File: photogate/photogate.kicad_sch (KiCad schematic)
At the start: 13 parts, among them P2_Jack_F(Leds)1 SJ1-3525N

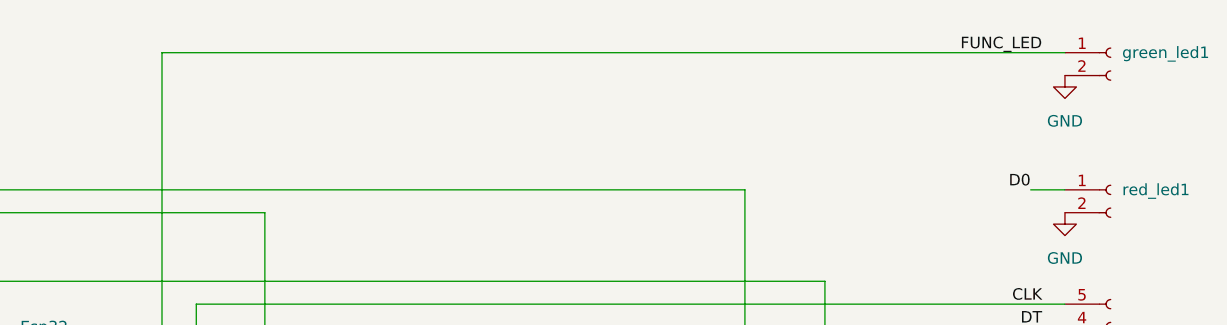
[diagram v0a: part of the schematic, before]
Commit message: Add resitor green led
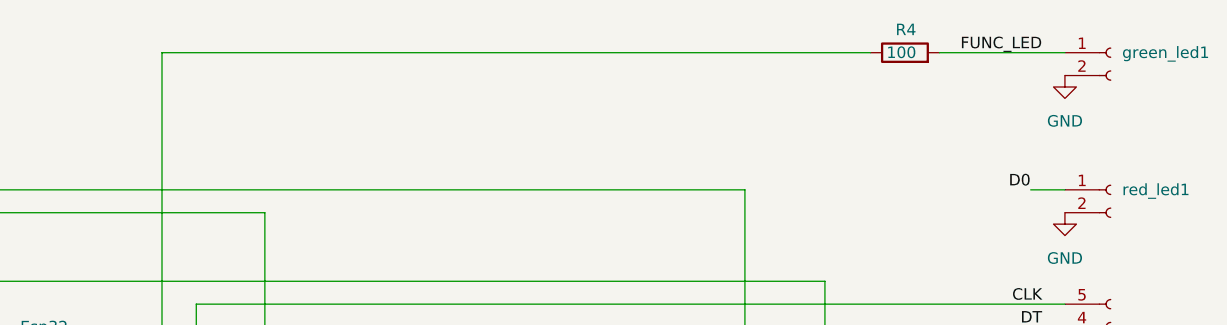
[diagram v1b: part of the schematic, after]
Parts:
- added R4: 100, Resistor_THT:R_Axial_DIN0204_L3.6mm_D1.6mm_P5.08mm_Horizontal, symbol Device:R
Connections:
- net FUNC_LED: now also R4.2; no longer Esp32.6 (IO32)
- new net: Esp32.6 (IO32), R4.1
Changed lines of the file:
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@@
     (stroke (width 0) (type default) (color 0 0 0 0))
   )
-  (wire (pts (xy 97.79 43.18) (xy 198.12 43.18))
+  (wire (pts (xy 97.79 43.18) (xy 176.53 43.18))
     (stroke (width 0) (type default) (color 0 0 0 0))
   )
   (wire (pts (xy 105.41 73.66) (xy 198.12 73.66))
+    (stroke (width 0) (type default) (color 0 0 0 0))
+  )
+  (wire (pts (xy 184.15 43.18) (xy 198.12 43.18))
     (stroke (width 0) (type default) (color 0 0 0 0))
   )
@@
     (pin "4")
   )
+  (symbol (lib_id "Device:R") (at 180.34 43.18 90) (unit 1)
+    (in_bom yes) (on_board yes)
+    (property "Reference" "R4" (id 0) (at 181.61 40.64 90)
+      (effects (font (size 1.27 1.27)) (justify left))
+    )
+    (property "Value" "100" (id 1) (at 181.61 43.18 90)
+      (effects (font (size 1.27 1.27)) (justify left))
+    )
+    (property "Footprint" "Resistor_THT:R_Axial_DIN0204_L3.6mm_D1.6mm_P5.08mm_Horizontal" (id 2) (at 180.34 44.958 90)
+      (effects (font (size 1.27 1.27)) hide)
+    )
+    (property "Datasheet" "~" (id 3) (at 180.34 43.18 0)
+      (effects (font (size 1.27 1.27)) hide)
+    )
+    (pin "1")
+    (pin "2")
+  )
   (symbol (lib_id "Connector:Conn_01x02_Female") (at 203.2 58.42 0) (unit 1)
     (in_bom yes) (on_board yes) (fields_autoplaced)
@@
       (reference "R3") (unit 1) (value "100") (footprint "Resistor_THT:R_Axial_DIN0204_L3.6mm_D1.6mm_P5.08mm_Horizontal")
     )
+    (path "/548078db-cb79-4624-8d94-1114d4729585"
+      (reference "R4") (unit 1) (value "100") (footprint "Resistor_THT:R_Axial_DIN0204_L3.6mm_D1.6mm_P5.08mm_Horizontal")
+    )
     (path "/63f1f18f-ec45-4294-bfb1-f0f704a6258f"

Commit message: Melhoras na placa
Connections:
- net D0: now also red_led1.2 (Pin_2); no longer red_led1.1 (Pin_1)
- net FUNC_LED: now also green_led1.2 (Pin_2); no longer green_led1.1 (Pin_1)
- net GND: now also green_led1.1 (Pin_1), red_led1.1 (Pin_1); no longer Esp32.17 (GND), green_led1.2 (Pin_2), red_led1.2 (Pin_2)
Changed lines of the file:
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@@
   (junction (at 198.12 110.49) (diameter 0) (color 0 0 0 0)
   )
-  (junction (at 80.01 147.32) (diameter 0) (color 0 0 0 0)
-  )
   (junction (at 171.45 124.46) (diameter 0) (color 0 0 0 0)
   )
@@
     (stroke (width 0) (type default) (color 0 0 0 0))
   )
+  (wire (pts (xy 194.31 58.42) (xy 198.12 58.42))
+    (stroke (width 0) (type default) (color 0 0 0 0))
+  )
   (wire (pts (xy 149.86 124.46) (xy 171.45 124.46))
     (stroke (width 0) (type default) (color 0 0 0 0))
   )
+  (wire (pts (xy 184.15 43.18) (xy 198.12 43.18))
+    (stroke (width 0) (type default) (color 0 0 0 0))
+  )
   (wire (pts (xy 198.12 110.49) (xy 198.12 113.03))
     (stroke (width 0) (type default) (color 0 0 0 0))
@@
     (stroke (width 0) (type default) (color 0 0 0 0))
   )
-  (wire (pts (xy 77.47 147.32) (xy 80.01 147.32))
+  (wire (pts (xy 77.47 147.32) (xy 139.7 147.32))
     (stroke (width 0) (type default) (color 0 0 0 0))
   )
@@
     (stroke (width 0) (type default) (color 0 0 0 0))
   )
-  (wire (pts (xy 184.15 43.18) (xy 198.12 43.18))
-    (stroke (width 0) (type default) (color 0 0 0 0))
-  )
   (wire (pts (xy 198.12 127) (xy 198.12 129.54))
     (stroke (width 0) (type default) (color 0 0 0 0))
@@
     (stroke (width 0) (type default) (color 0 0 0 0))
   )
-  (wire (pts (xy 194.31 58.42) (xy 198.12 58.42))
-    (stroke (width 0) (type default) (color 0 0 0 0))
-  )
   (wire (pts (xy 139.7 124.46) (xy 139.7 127))
     (stroke (width 0) (type default) (color 0 0 0 0))
   )
   (wire (pts (xy 95.25 137.16) (xy 105.41 137.16))
-    (stroke (width 0) (type default) (color 0 0 0 0))
-  )
-  (wire (pts (xy 80.01 147.32) (xy 139.7 147.32))
     (stroke (width 0) (type default) (color 0 0 0 0))
   )
@@
     (pin "2")
   )
-  (symbol (lib_id "Connector:Conn_01x02_Female") (at 203.2 58.42 0) (unit 1)
-    (in_bom yes) (on_board yes) (fields_autoplaced)
-    (property "Reference" "red_led1" (id 0) (at 204.47 58.4199 0)
-      (effects (font (size 1.27 1.27)) (justify left))
-    )
-    (property "Value" "Conn_01x02_Female" (id 1) (at 204.47 60.9599 0)
+  (symbol (lib_id "Connector:Conn_01x02_Female") (at 203.2 60.96 0) (mirror x) (unit 1)
+    (in_bom yes) (on_board yes) (fields_autoplaced)
+    (property "Reference" "red_led1" (id 0) (at 202.565 55.88 0))
+    (property "Value" "Conn_01x02_Female" (id 1) (at 204.47 58.4201 0)
       (effects (font (size 1.27 1.27)) (justify left) hide)
     )
-    (property "Footprint" "Connector_JST:JST_EH_B2B-EH-A_1x02_P2.50mm_Vertical" (id 2) (at 203.2 58.42 0)
-      (effects (font (size 1.27 1.27)) hide)
-    )
-    (property "Datasheet" "~" (id 3) (at 203.2 58.42 0)
+    (property "Footprint" "Connector_JST:JST_EH_B2B-EH-A_1x02_P2.50mm_Vertical" (id 2) (at 203.2 60.96 0)
+      (effects (font (size 1.27 1.27)) hide)
+    )
+    (property "Datasheet" "~" (id 3) (at 203.2 60.96 0)
       (effects (font (size 1.27 1.27)) hide)
     )
@@
     (pin "1")
   )
-  (symbol (lib_id "Connector:Conn_01x02_Female") (at 203.2 43.18 0) (unit 1)
-    (in_bom yes) (on_board yes)
-    (property "Reference" "green_led1" (id 0) (at 204.47 43.18 0)
-      (effects (font (size 1.27 1.27)) (justify left))
-    )
-    (property "Value" "Conn_01x02_Female" (id 1) (at 204.47 45.7199 0)
+  (symbol (lib_id "Connector:Conn_01x02_Female") (at 203.2 45.72 0) (mirror x) (unit 1)
+    (in_bom yes) (on_board yes)
+    (property "Reference" "green_led1" (id 0) (at 209.55 45.72 0)
+      (effects (font (size 1.27 1.27)) (justify left))
+    )
+    (property "Value" "Conn_01x02_Female" (id 1) (at 204.47 43.1801 0)
       (effects (font (size 1.27 1.27)) (justify left) hide)
     )
-    (property "Footprint" "Connector_JST:JST_EH_B2B-EH-A_1x02_P2.50mm_Vertical" (id 2) (at 203.2 43.18 0)
-      (effects (font (size 1.27 1.27)) hide)
-    )
-    (property "Datasheet" "~" (id 3) (at 203.2 43.18 0)
-      (effects (font (size 1.27 1.27)) hide)
-    )
+    (property "Footprint" "Connector_JST:JST_EH_B2B-EH-A_1x02_P2.50mm_Vertical" (id 2) (at 203.2 45.72 0)
+      (effects (font (size 1.27 1.27)) hide)
+    )
+    (property "Datasheet" "~" (id 3) (at 203.2 45.72 0)
+      (effects (font (size 1.27 1.27)) hide)
+    )

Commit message: att designe PCB
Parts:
- removed P2_Jack_F(Leds)1: SJ1-3525N, MyFootprints:CUI_SJ1-3525N, symbol Jacks:SJ1-3525N
- added P2jack1: SJ1-3515N, MyFootprints:CUI_SJ1-3515N, symbol MySymbols:SJ1-3515N
- added R5: 470, Resistor_THT:R_Axial_DIN0204_L3.6mm_D1.6mm_P7.62mm_Horizontal, symbol Device:R
- C1: value 104 -> 104k; footprint Capacitor_THT:C_Disc_D5.1mm_W3.2mm_P5.00mm -> Capacitor_THT:C_Disc_D10.5mm_W5.0mm_P10.00mm
- LM393N_A1: value LM393N_A -> LM393N1
- R1: renamed from R4; footprint Resistor_THT:R_Axial_DIN0204_L3.6mm_D1.6mm_P5.08mm_Horizontal -> Resistor_THT:R_Axial_DIN0204_L3.6mm_D1.6mm_P7.62mm_Horizontal
- R2: renamed from R3; footprint Resistor_THT:R_Axial_DIN0204_L3.6mm_D1.6mm_P5.08mm_Horizontal -> Resistor_THT:R_Axial_DIN0204_L3.6mm_D1.6mm_P7.62mm_Horizontal
- R3: renamed from R1; footprint Resistor_THT:R_Axial_DIN0204_L3.6mm_D1.6mm_P5.08mm_Horizontal -> Resistor_THT:R_Axial_DIN0204_L3.6mm_D1.6mm_P7.62mm_Horizontal
- R4: renamed from R2; footprint Resistor_THT:R_Axial_DIN0204_L3.6mm_D1.6mm_P5.08mm_Horizontal -> Resistor_THT:R_Axial_DIN0204_L3.6mm_D1.6mm_P7.62mm_Horizontal
- renumbered VR10kteste1 to VR1
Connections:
- net D0: now also R5.1; no longer red_led1.2 (Pin_2)
- net GND: now also Esp32.17 (GND), P2jack1.2, P2jack1.4
- net PHOTODIODE: now also P2jack1.1
- net at Esp32.15 (VIN), Jack_5V1.4, R3.1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: no longer C1.1, LM393N_A1.8 (V+), R2.2, R4.1, VR1.1
- net at Esp32.16 (3V3): now also C1.1, LM393N_A1.8 (V+), R4.1, VR1.1, R5.2
- net at R3.2: now also P2jack1.3, P2jack1.5
- new net: R2.2, red_led1.2 (Pin_2)
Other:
- moved on the sheet: R2, R4, VR1

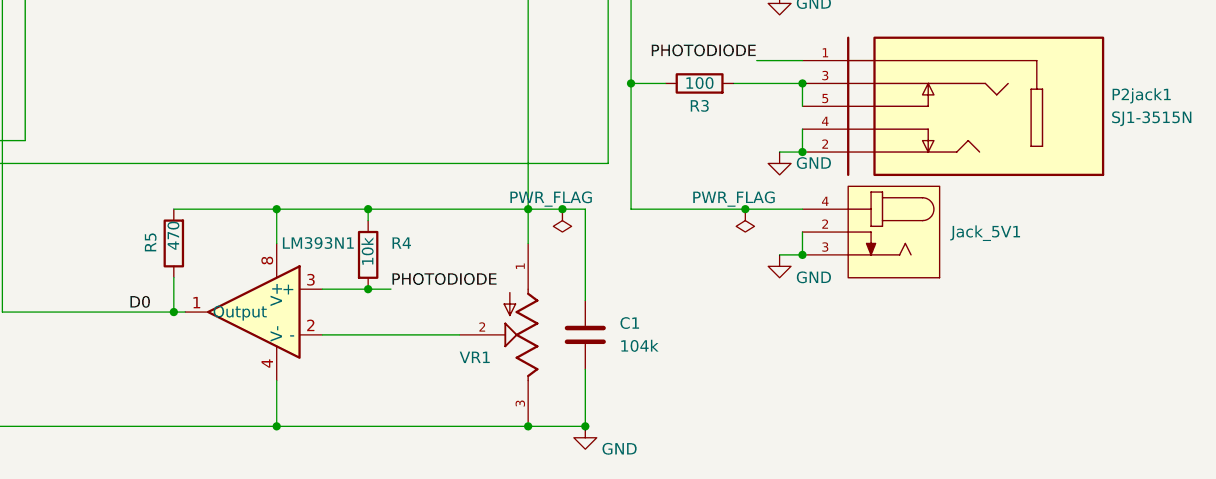
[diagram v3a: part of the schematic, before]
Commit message: Add connector para switch
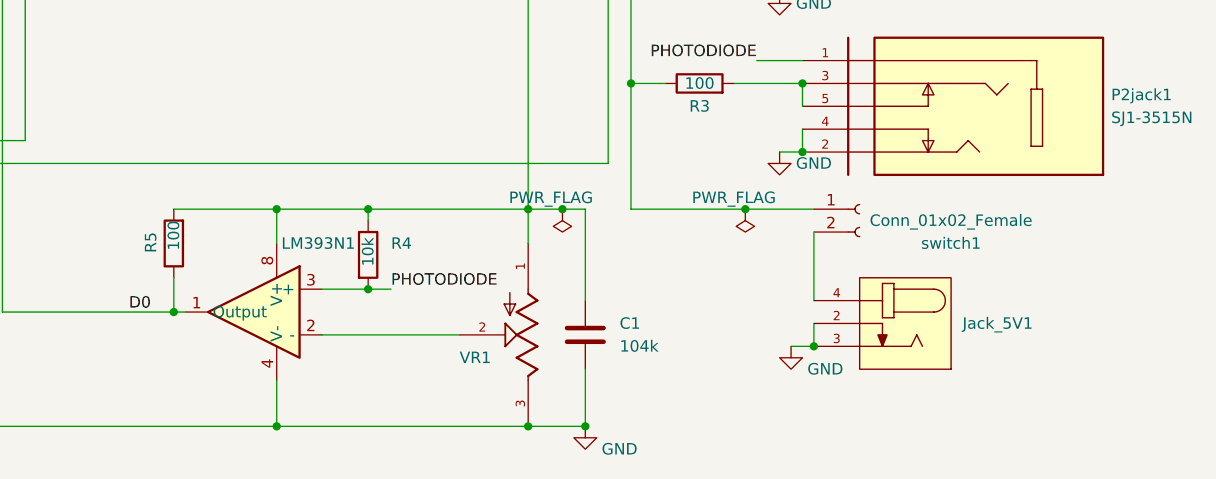
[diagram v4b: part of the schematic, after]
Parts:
- added switch1: Conn_01x02_Female, Connector_JST:JST_EH_B2B-EH-A_1x02_P2.50mm_Vertical, symbol Connector:Conn_01x02_Female
- R5: value 470 -> 100
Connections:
- net at Esp32.15 (VIN), R3.1, display1.2 (Pin_2)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: now also switch1.1 (Pin_1); no longer Jack_5V1.4
- new net: Jack_5V1.4, switch1.2 (Pin_2)
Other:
- moved on the sheet: Jack_5V1
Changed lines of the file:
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@@
   (junction (at 179.07 78.74) (diameter 0) (color 0 0 0 0)
   )
-  (junction (at 198.12 129.54) (diameter 0) (color 0 0 0 0)
+  (junction (at 199.39 139.7) (diameter 0) (color 0 0 0 0)
   )
   (junction (at 139.7 148.59) (diameter 0) (color 0 0 0 0)
@@
   (junction (at 167.64 148.59) (diameter 0) (color 0 0 0 0)
   )
+  (junction (at 198.12 118.11) (diameter 0) (color 0 0 0 0)
+  )
+  (junction (at 77.47 147.32) (diameter 0) (color 0 0 0 0)
+  )
+  (junction (at 173.99 148.59) (diameter 0) (color 0 0 0 0)
+  )
   (junction (at 191.77 124.46) (diameter 0) (color 0 0 0 0)
   )
-  (junction (at 198.12 118.11) (diameter 0) (color 0 0 0 0)
-  )
-  (junction (at 77.47 147.32) (diameter 0) (color 0 0 0 0)
-  )
-  (junction (at 173.99 148.59) (diameter 0) (color 0 0 0 0)
-  )
   (junction (at 167.64 124.46) (diameter 0) (color 0 0 0 0)
   )
@@
     (stroke (width 0) (type default) (color 0 0 0 0))
   )
+  (wire (pts (xy 199.39 127) (xy 199.39 134.62))
+    (stroke (width 0) (type default) (color 0 0 0 0))
+  )
   (wire (pts (xy 149.86 124.46) (xy 167.64 124.46))
     (stroke (width 0) (type default) (color 0 0 0 0))
@@
     (stroke (width 0) (type default) (color 0 0 0 0))
   )
-  (wire (pts (xy 191.77 124.46) (xy 198.12 124.46))
-    (stroke (width 0) (type default) (color 0 0 0 0))
-  )
   (wire (pts (xy 139.7 124.46) (xy 149.86 124.46))
     (stroke (width 0) (type default) (color 0 0 0 0))
@@
     (stroke (width 0) (type default) (color 0 0 0 0))
   )
-  (wire (pts (xy 198.12 127) (xy 198.12 129.54))
+  (wire (pts (xy 199.39 137.16) (xy 199.39 139.7))
     (stroke (width 0) (type default) (color 0 0 0 0))
   )
@@
     (stroke (width 0) (type default) (color 0 0 0 0))
   )
-  (wire (pts (xy 195.58 129.54) (xy 198.12 129.54))
+  (wire (pts (xy 196.85 139.7) (xy 199.39 139.7))
     (stroke (width 0) (type default) (color 0 0 0 0))
   )
@@
   )
   (wire (pts (xy 95.25 119.38) (xy 176.53 119.38))
+    (stroke (width 0) (type default) (color 0 0 0 0))
+  )
+  (wire (pts (xy 191.77 124.46) (xy 199.39 124.46))
     (stroke (width 0) (type default) (color 0 0 0 0))
   )
@@
     (pin "9")
   )
-  (symbol (lib_id "power:GND") (at 195.58 129.54 0) (unit 1)
-    (in_bom yes) (on_board yes)
-    (property "Reference" "#PWR0102" (id 0) (at 195.58 135.89 0)
-      (effects (font (size 1.27 1.27)) hide)
-    )
-    (property "Value" "GND" (id 1) (at 199.39 132.08 0))
-    (property "Footprint" "" (id 2) (at 195.58 129.54 0)
-      (effects (font (size 1.27 1.27)) hide)
-    )
-    (property "Datasheet" "" (id 3) (at 195.58 129.54 0)
+  (symbol (lib_id "power:GND") (at 196.85 139.7 0) (unit 1)
+    (in_bom yes) (on_board yes)
+    (property "Reference" "#PWR0102" (id 0) (at 196.85 146.05 0)
+      (effects (font (size 1.27 1.27)) hide)
+    )
+    (property "Value" "GND" (id 1) (at 200.66 142.24 0))
+    (property "Footprint" "" (id 2) (at 196.85 139.7 0)
+      (effects (font (size 1.27 1.27)) hide)
+    )
+    (property "Datasheet" "" (id 3) (at 196.85 139.7 0)
       (effects (font (size 1.27 1.27)) hide)
     )
@@
       (effects (font (size 1.27 1.27)) (justify left))
     )
-    (property "Value" "470" (id 1) (at 128.27 125.73 90)
+    (property "Value" "100" (id 1) (at 128.27 125.73 90)
       (effects (font (size 1.27 1.27)) (justify left))
     )
@@
     (pin "8")
   )
-  (symbol (lib_id "Jacks:DC-005") (at 208.28 127 0) (mirror y) (unit 1)
+  (symbol (lib_id "Jacks:DC-005") (at 209.55 137.16 0) (mirror y) (unit 1)
     (in_bom yes) (on_board yes) (fields_autoplaced)
-    (property "Reference" "Jack_5V1" (id 0) (at 214.63 126.9999 0)
+    (property "Reference" "Jack_5V1" (id 0) (at 215.9 137.1599 0)
       (effects (font (size 1.27 1.27)) (justify right))
     )
-    (property "Value" "DC-005" (id 1) (at 214.63 128.2699 0)
+    (property "Value" "DC-005" (id 1) (at 215.9 138.4299 0)
       (effects (font (size 1.27 1.27)) (justify right) hide)
     )
-    (property "Footprint" "MyFootprints:NINIGI_DC-005" (id 2) (at 208.28 137.16 0)
-      (effects (font (size 1.27 1.27)) hide)
-    )
-    (property "Datasheet" "" (id 3) (at 208.28 127 0)
-      (effects (font (size 1.27 1.27)) hide)
-    )
-    (property "DESCRIPTION" "Conn Dc Power Jack 2.1mm" (id 4) (at 208.28 118.11 0)
+    (property "Footprint" "MyFootprints:NINIGI_DC-005" (id 2) (at 209.55 147.32 0)
+      (effects (font (size 1.27 1.27)) hide)
+    )
+    (property "Datasheet" "" (id 3) (at 209.55 137.16 0)
+      (effects (font (size 1.27 1.27)) hide)
+    )
+    (property "DESCRIPTION" "Conn Dc Power Jack 2.1mm" (id 4) (at 209.55 128.27 0)
       (effects (font (size 1.27 1.27)) (justify bottom) hide)
     )
@@
     )
     (property "Datasheet" "~" (id 3) (at 149.86 129.54 0)
+      (effects (font (size 1.27 1.27)) hide)
+    )
+    (pin "1")
+    (pin "2")
+  )
+  (symbol (lib_id "Connector:Conn_01x02_Female") (at 204.47 124.46 0) (unit 1)
+    (in_bom yes) (on_board yes)
+    (property "Reference" "switch1" (id 0) (at 214.63 128.27 0))
+    (property "Value" "Conn_01x02_Female" (id 1) (at 214.63 125.73 0))
+    (property "Footprint" "Connector_JST:JST_EH_B2B-EH-A_1x02_P2.50mm_Vertical" (id 2) (at 204.47 124.46 0)
+      (effects (font (size 1.27 1.27)) hide)
+    )
+    (property "Datasheet" "~" (id 3) (at 204.47 124.46 0)
       (effects (font (size 1.27 1.27)) hide)
     )
@@
     )
     (path "/32cb601b-1a23-4123-bcc0-c2e3f0d8b576"
-      (reference "R5") (unit 1) (value "470") (footprint "Resistor_THT:R_Axial_DIN0204_L3.6mm_D1.6mm_P7.62mm_Horizontal")
+      (reference "R5") (unit 1) (value "100") (footprint "Resistor_THT:R_Axial_DIN0204_L3.6mm_D1.6mm_P7.62mm_Horizontal")
     )
     (path "/63f1f18f-ec45-4294-bfb1-f0f704a6258f"
@@
       (reference "red_led1") (unit 1) (value "Conn_01x02_Female") (footprint "Connector_JST:JST_EH_B2B-EH-A_1x02_P2.50mm_Vertical")
     )
-  )
+    (path "/d107a962-f6e5-4ac7-b141-1217862cb864"
+      (reference "switch1") (unit 1) (value "Conn_01x02_Female") (footprint "Connector_JST:JST_EH_B2B-EH-A_1x02_P2.50mm_Vertical")
+    )
+  )

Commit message: Trocar connector jst para KK
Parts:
- display1: footprint Connector_JST:JST_EH_B4B-EH-A_1x04_P2.50mm_Vertical -> Connector_Molex:Molex_KK-254_AE-6410-04A_1x04_P2.54mm_Vertical
- enconder1: footprint Connector_JST:JST_EH_B5B-EH-A_1x05_P2.50mm_Vertical -> Connector_Molex:Molex_KK-254_AE-6410-05A_1x05_P2.54mm_Vertical
- green_led1, red_led1, switch1: footprint Connector_JST:JST_EH_B2B-EH-A_1x02_P2.50mm_Vertical -> Connector_Molex:Molex_KK-254_AE-6410-02A_1x02_P2.54mm_Vertical
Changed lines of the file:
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@@
       (effects (font (size 1.27 1.27)) (justify left) hide)
     )
-    (property "Footprint" "Connector_JST:JST_EH_B4B-EH-A_1x04_P2.50mm_Vertical" (id 2) (at 203.2 97.79 0)
+    (property "Footprint" "Connector_Molex:Molex_KK-254_AE-6410-04A_1x04_P2.54mm_Vertical" (id 2) (at 203.2 97.79 0)
       (effects (font (size 1.27 1.27)) hide)
     )
@@
       (effects (font (size 1.27 1.27)) (justify left) hide)
     )
-    (property "Footprint" "Connector_JST:JST_EH_B2B-EH-A_1x02_P2.50mm_Vertical" (id 2) (at 203.2 60.96 0)
+    (property "Footprint" "Connector_Molex:Molex_KK-254_AE-6410-02A_1x02_P2.54mm_Vertical" (id 2) (at 203.2 60.96 0)
       (effects (font (size 1.27 1.27)) hide)
     )
@@
       (effects (font (size 1.27 1.27)) (justify left) hide)
     )
-    (property "Footprint" "Connector_JST:JST_EH_B5B-EH-A_1x05_P2.50mm_Vertical" (id 2) (at 203.2 76.2 0)
+    (property "Footprint" "Connector_Molex:Molex_KK-254_AE-6410-05A_1x05_P2.54mm_Vertical" (id 2) (at 203.2 76.2 0)
       (effects (font (size 1.27 1.27)) hide)
     )
@@
     (property "Reference" "switch1" (id 0) (at 214.63 128.27 0))
     (property "Value" "Conn_01x02_Female" (id 1) (at 214.63 125.73 0))
-    (property "Footprint" "Connector_JST:JST_EH_B2B-EH-A_1x02_P2.50mm_Vertical" (id 2) (at 204.47 124.46 0)
+    (property "Footprint" "Connector_Molex:Molex_KK-254_AE-6410-02A_1x02_P2.54mm_Vertical" (id 2) (at 204.47 124.46 0)
       (effects (font (size 1.27 1.27)) hide)
     )
@@
       (effects (font (size 1.27 1.27)) (justify left) hide)
     )
-    (property "Footprint" "Connector_JST:JST_EH_B2B-EH-A_1x02_P2.50mm_Vertical" (id 2) (at 203.2 45.72 0)
+    (property "Footprint" "Connector_Molex:Molex_KK-254_AE-6410-02A_1x02_P2.54mm_Vertical" (id 2) (at 203.2 45.72 0)
       (effects (font (size 1.27 1.27)) hide)
     )
@@
     )
     (path "/52fccdab-71de-4b70-a7c9-485da3fafee0"
-      (reference "display1") (unit 1) (value "Conn_01x04_Female") (footprint "Connector_JST:JST_EH_B4B-EH-A_1x04_P2.50mm_Vertical")
+      (reference "display1") (unit 1) (value "Conn_01x04_Female") (footprint "Connector_Molex:Molex_KK-254_AE-6410-04A_1x04_P2.54mm_Vertical")
     )
     (path "/5fb0064b-5d27-40c3-be50-cd9760b03f21"
-      (reference "enconder1") (unit 1) (value "Conn_01x05_Female") (footprint "Connector_JST:JST_EH_B5B-EH-A_1x05_P2.50mm_Vertical")
+      (reference "enconder1") (unit 1) (value "Conn_01x05_Female") (footprint "Connector_Molex:Molex_KK-254_AE-6410-05A_1x05_P2.54mm_Vertical")
     )
     (path "/ff52656d-9062-4621-88b0-14400ecd07e5"
-      (reference "green_led1") (unit 1) (value "Conn_01x02_Female") (footprint "Connector_JST:JST_EH_B2B-EH-A_1x02_P2.50mm_Vertical")
+      (reference "green_led1") (unit 1) (value "Conn_01x02_Female") (footprint "Connector_Molex:Molex_KK-254_AE-6410-02A_1x02_P2.54mm_Vertical")
     )
     (path "/54b3576d-9fde-46e8-97ef-e9aae314452b"
-      (reference "red_led1") (unit 1) (value "Conn_01x02_Female") (footprint "Connector_JST:JST_EH_B2B-EH-A_1x02_P2.50mm_Vertical")
+      (reference "red_led1") (unit 1) (value "Conn_01x02_Female") (footprint "Connector_Molex:Molex_KK-254_AE-6410-02A_1x02_P2.54mm_Vertical")
     )
     (path "/d107a962-f6e5-4ac7-b141-1217862cb864"
-      (reference "switch1") (unit 1) (value "Conn_01x02_Female") (footprint "Connector_JST:JST_EH_B2B-EH-A_1x02_P2.50mm_Vertical")
-    )
-  )
+      (reference "switch1") (unit 1) (value "Conn_01x02_Female") (footprint "Connector_Molex:Molex_KK-254_AE-6410-02A_1x02_P2.54mm_Vertical")
+    )
+  )

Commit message: Ultimos ajustes
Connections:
- net GND: now also P2jack1.1; no longer P2jack1.2, P2jack1.4
- net PHOTODIODE: now also P2jack1.2; no longer P2jack1.1
- net at P2jack1.3, R3.2: no longer P2jack1.5
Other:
- moved on the sheet: R3
